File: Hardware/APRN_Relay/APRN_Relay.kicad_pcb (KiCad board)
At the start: 2 copper layers, 64 x 56 mm, 44 parts, among them J101 SERVO1, J102 SERVO2, J103 PTT, J104 Pi_Zero, J105 RADIO, J106 CHG, J107 PWR, J108 BAT, U101 DHT11, U102 INA219AIDR, U103 NCV1117ST50T3G

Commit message: Add PTT DNP
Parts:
- added JP1: SolderJumper_2_Bridged, Jumper:SolderJumper-2_P1.3mm_Bridged_Pad1.0x1.5mm, F.Cu at (161.2, 84.2)
- added R1: DNP, Resistor_SMD:R_0805_2012Metric, F.Cu at (158.8, 86.8)
- renumbered C101 to C1, C102 to C2, C103 to C3, C104 to C4, C105 to C5, D101 to D1, D102 to D2, D103 to D3, D104 to D4, D105 to D5, H101 to H1, H102 to H2, H103 to H3, H104 to H4, H105 to H5, H106 to H6, J101 to J1, J102 to J2, J103 to J3, J104 to J4, J105 to J5, J106 to J6, J107 to J7, J108 to J8, JP101 to JP2, JP102 to JP3, JP103 to JP4, R111 to R10, R109 to R11, R110 to R12, R101 to R2, R102 to R3, R103 to R4, R104 to R5, R105 to R6, R106 to R7, R107 to R8, R108 to R9, U101 to U1, U102 to U2, U103 to U3
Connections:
- J3 pad 2: /TX -> Net-(J3-Pad2)
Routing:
- net Net-(J3-Pad2): track 0.00 -> 12.9 mm
- net /TX: track 85.0 -> 78.2 mm

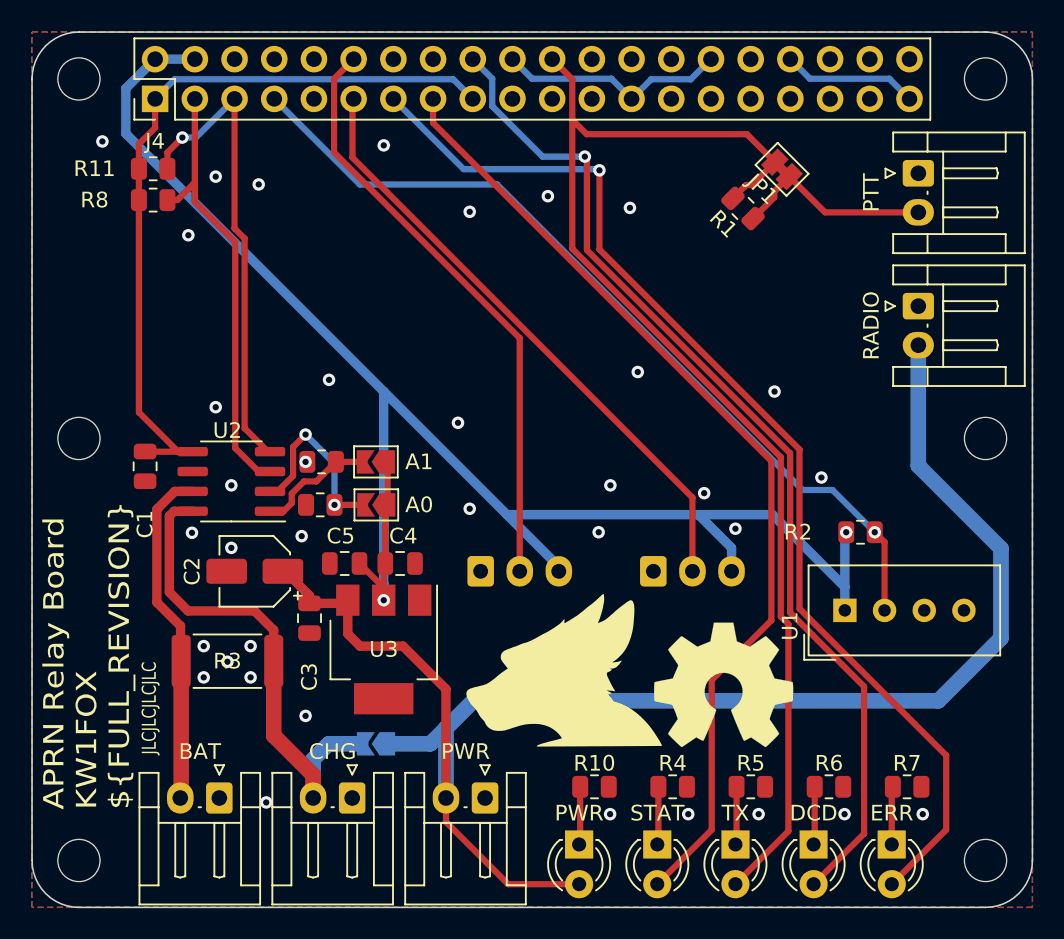
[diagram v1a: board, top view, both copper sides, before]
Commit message: bump with new plugs on the back
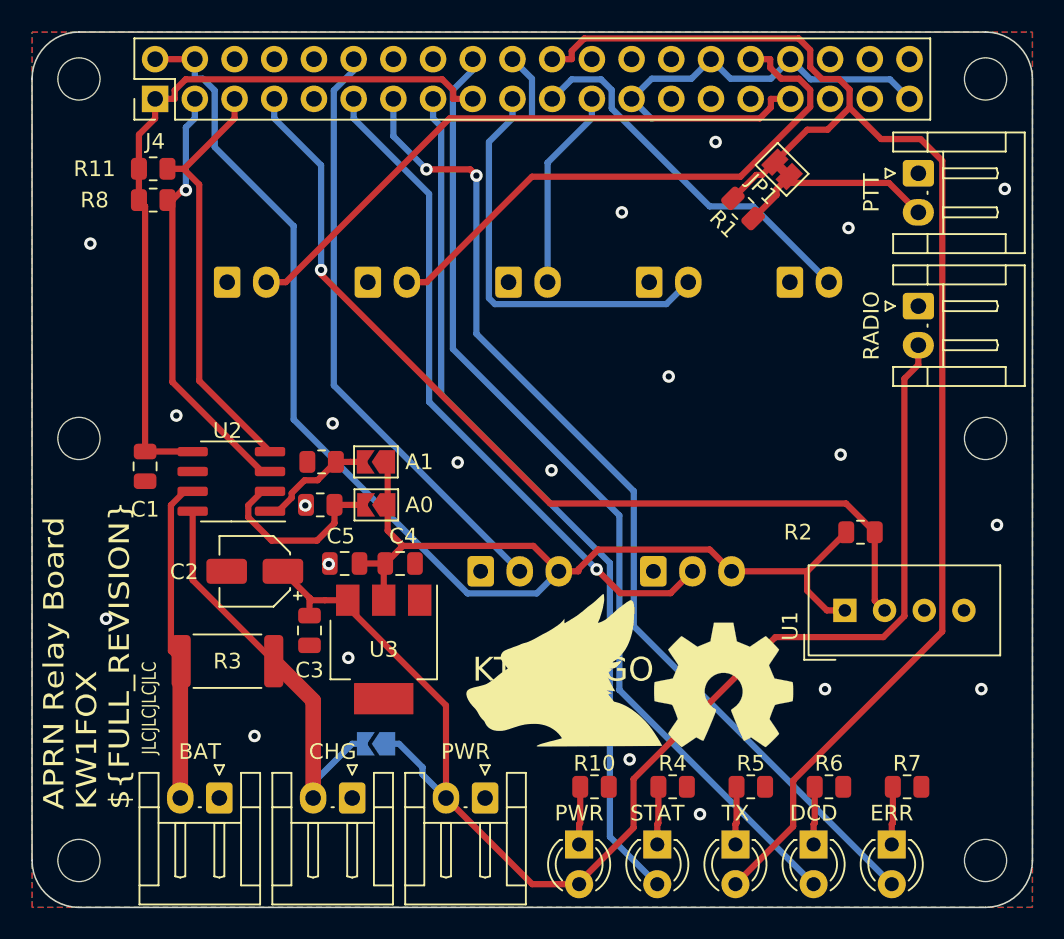
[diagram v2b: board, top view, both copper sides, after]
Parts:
- added J101: GP13, Connector_JST:JST_EH_S2B-EH_1x02_P2.50mm_Horizontal, B.Cu at (125.8, 91.5)
- added J102: GP9, Connector_JST:JST_EH_S2B-EH_1x02_P2.50mm_Horizontal, B.Cu at (161.8, 91.5)
- added J103: GP10, Connector_JST:JST_EH_S2B-EH_1x02_P2.50mm_Horizontal, B.Cu at (152.8, 91.5)
- added J104: GP11, Connector_JST:JST_EH_S2B-EH_1x02_P2.50mm_Horizontal, B.Cu at (143.8, 91.5)
- added J105: GP12, Connector_JST:JST_EH_S2B-EH_1x02_P2.50mm_Horizontal, B.Cu at (134.8, 91.5)
- C1, C5: value 1uF -> 1μf
- C2: value 10uf -> 10μf
- C3, C4: value 100nF -> 0.1μf
- moved C3 0.79 mm to (131.0, 113.8)
- renumbered REF** to KICADLOGO, G*** to KTSNLOGO, REF** to OSHWLOGO
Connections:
- J4 pad 19: unconnected-(J4-Pad19) -> /GPIO10
- J4 pad 21: unconnected-(J4-Pad21) -> /GPIO9
- J4 pad 23: unconnected-(J4-Pad23) -> /GPIO11
- J4 pad 32: unconnected-(J4-Pad32) -> /GPIO12
- J4 pad 33: unconnected-(J4-Pad33) -> /GPIO13
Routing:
- net /GPIO13: track 0.00 -> 38.7 mm
- net /GPIO12: track 0.00 -> 36.5 mm
- net /GPIO10: track 0.00 -> 26.9 mm
- net /GPIO9: track 0.00 -> 24.3 mm
- net /POWER: track 101.4 -> 85.8 mm
- net /TX: track 78.2 -> 92.0 mm
- net /GPIO11: track 0.00 -> 12.9 mm
- net +5V: track 105.9 -> 97.5 mm, vias 2 -> 0
- net /ERR: track 71.4 -> 65.1 mm, vias 1 -> 2
- net /STAT: track 62.2 -> 56.2 mm
- net /CHARGE: track 31.9 -> 26.8 mm
- net /DHT_DATA: track 55.2 -> 60.0 mm
- net /SERVO2: track 39.3 -> 43.9 mm, vias 0 -> 1
- net GND: track 23.5 -> 26.9 mm, vias 36 -> 21
- net /DCD: track 66.1 -> 62.9 mm, vias 1 -> 0
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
